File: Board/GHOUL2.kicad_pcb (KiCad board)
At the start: 2 copper layers, 105.4 x 88.9 mm, 37 parts

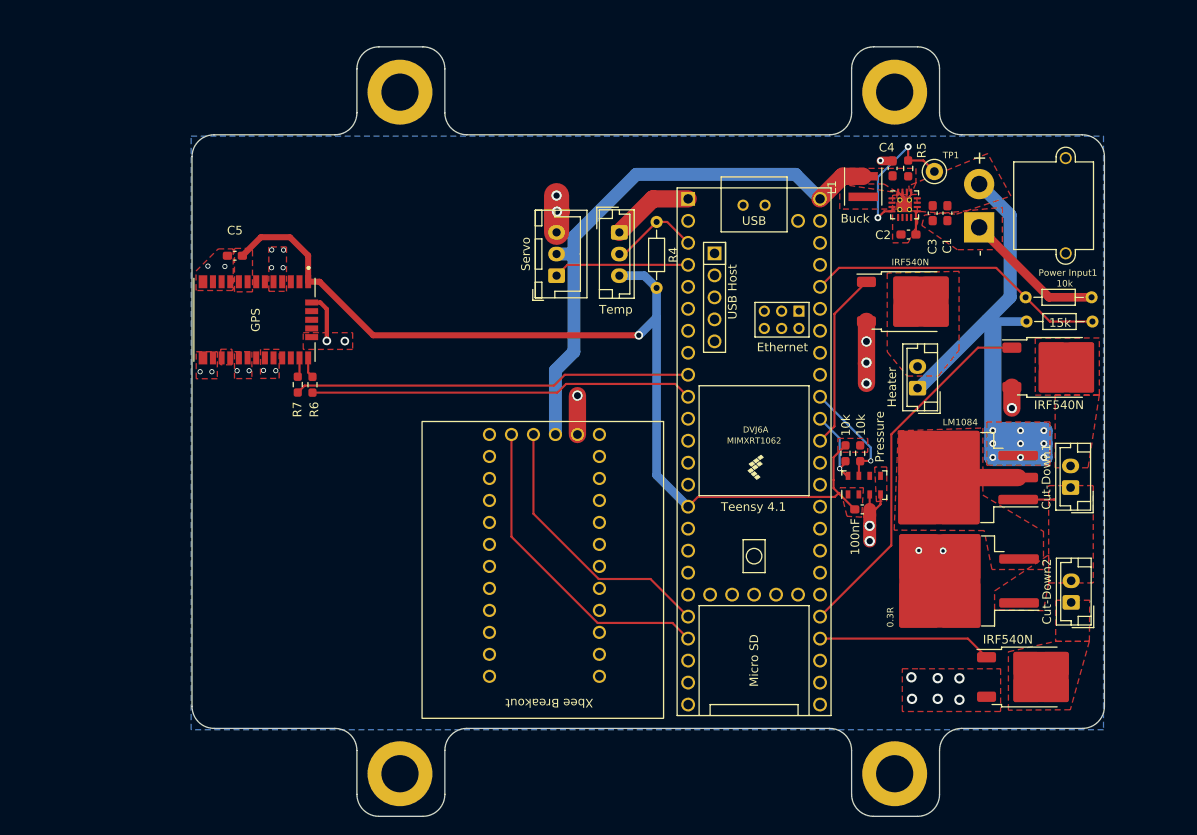
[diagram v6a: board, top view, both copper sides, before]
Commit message: added SAM and changed PCB
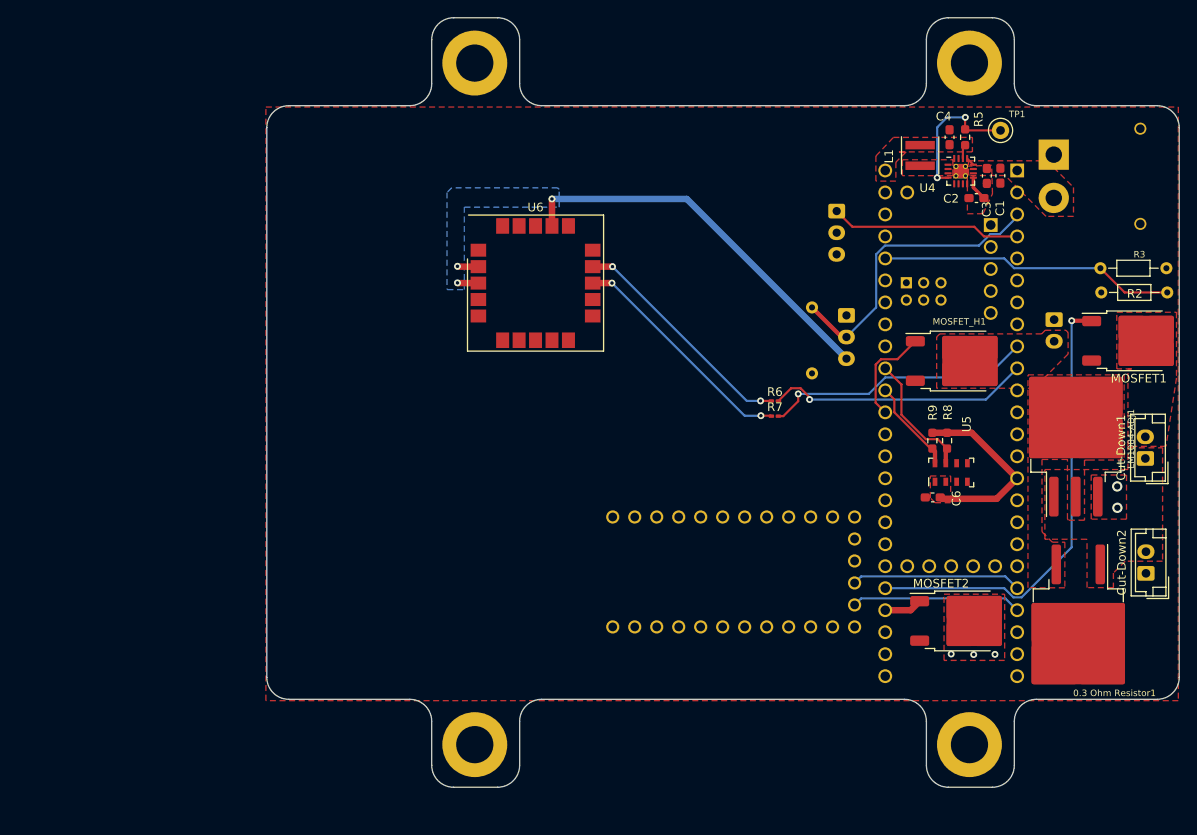
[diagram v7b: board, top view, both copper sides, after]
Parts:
- removed C5: 4.7uF, Capacitor_SMD:C_0603_1608Metric_Pad1.08x0.95mm_HandSolder
- removed GPS: CAM-M8Q-0, CAM-M8Q-0:LCC100P960X1400X210-31N
- added U6: SAM-M8Q, RF_GPS:ublox_SAM-M8Q, F.Cu at (133.8, 85.6)
- 0.3 Ohm Resistor1: renamed from 0.3R
- M1: renamed from Servo; moved to B.Cu
- Power Input1: moved to B.Cu
- R1: renamed from Heater; moved to B.Cu
- R2: renamed from 15k; value 15K -> 15k
- R4: moved to B.Cu
- R6, R7: value 220 -> R220; footprint Resistor_SMD:R_0603_1608Metric_Pad0.98x0.95mm_HandSolder -> Resistor_SMD:R_0201_0603Metric_Pad0.64x0.40mm_HandSolder
- U1: renamed from Teensy 4.1; moved to B.Cu
- U2: renamed from Temp; moved to B.Cu
- Xbee Breakout1: renamed from Xbee Breakout; moved to B.Cu
- moved R7 55.2 mm to (161.4, 100.9), turned to 0 degrees
- moved R6 53.5 mm to (161.4, 99.2), turned to 0 degrees
- moved M1 33.2 mm to (168.6, 77.2), turned to -90 degrees
- moved U2 27.9 mm to (169.7, 89.3)
- moved Xbee Breakout1 23.8 mm to (172.1, 105.2), turned to -90 degrees
- moved U1 23.0 mm to (181.8, 101.8)
- moved R4 20.5 mm to (165.7, 88.4)
- moved G*** 18.0 mm to (142.1, 91.8), turned to 0 degrees
- moved R1 17.7 mm to (193.7, 89.8), turned to -90 degrees
- moved 0.3 Ohm Resistor1 15.6 mm to (196.5, 125.7), turned to -90 degrees
- moved LM1084-ADJ1 15.3 mm to (196.2, 102.6), turned to 90 degrees
- moved Power Input1 12.0 mm to (193.6, 70.7), turned to 90 degrees
- moved R9 10.1 mm to (179.6, 103.8)
- moved R8 10.1 mm to (181.3, 103.8)
- moved U5 10.1 mm to (181.8, 107.4)
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- renumbered 100nF to C6, LM1084 to LM1084-ADJ1, IRF540N to MOSFET1, IRF540N to MOSFET2, IRF540N to MOSFET_H1, 10k to R3, 10k to R8, 10k to R9, Buck to U4, Pressure to U5
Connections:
- R6 pad 1: GPSRx -> Net-(U6-RXD)
- R6 pad 2: Net-(U3-RXD/SPI_MOSI) -> GPSRx
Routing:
- net +BATT: track 71.4 -> 1.01 mm, vias 9 -> 2
- net +5V: track 64.4 -> 1.65 mm
- net GND: track 63.1 -> 0.40 mm, vias 32 -> 0
- net +3.3V: track 114.7 -> 71.6 mm, vias 1 -> 3
- net Net-(U6-RXD): track 0.00 -> 27.1 mm, vias 0 -> 2
- net Net-(U6-TXD): track 2.26 -> 27.0 mm, vias 0 -> 2
- net Temp_Data: track 10.5 -> 34.7 mm
- net Xbee DIn: track 37.1 -> 19.7 mm
- net Nic2: track 20.1 -> 4.41 mm
- net GPSTx: track 45.9 -> 31.4 mm, vias 0 -> 1
- net GPSRx: track 44.4 -> 30.4 mm, vias 0 -> 1
- net Xbee DOut: track 31.9 -> 19.7 mm
- net Nic1: track 42.5 -> 52.9 mm, vias 0 -> 1
- net Net-(MOSFET_H1-G): track 20.6 -> 11.7 mm
- net Net-(LM1084-ADJ1-VO): track 9.15 -> 0.78 mm
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- added copper zone on B.Cu, net +3.3V
- added copper zone on In2.Cu, net +3.3V
- added copper zone on In2.Cu, net +5V
- added copper zone on In2.Cu, net +BATT
- added copper zone on In1.Cu, net GND
- added copper zone on In2.Cu, net Net-(Cut-Down2-In)
- removed copper zone on B.Cu, net GND
- removed copper zone on F.Cu, net Net-(U3-RF_IN)
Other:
- copper layers 2 -> 4

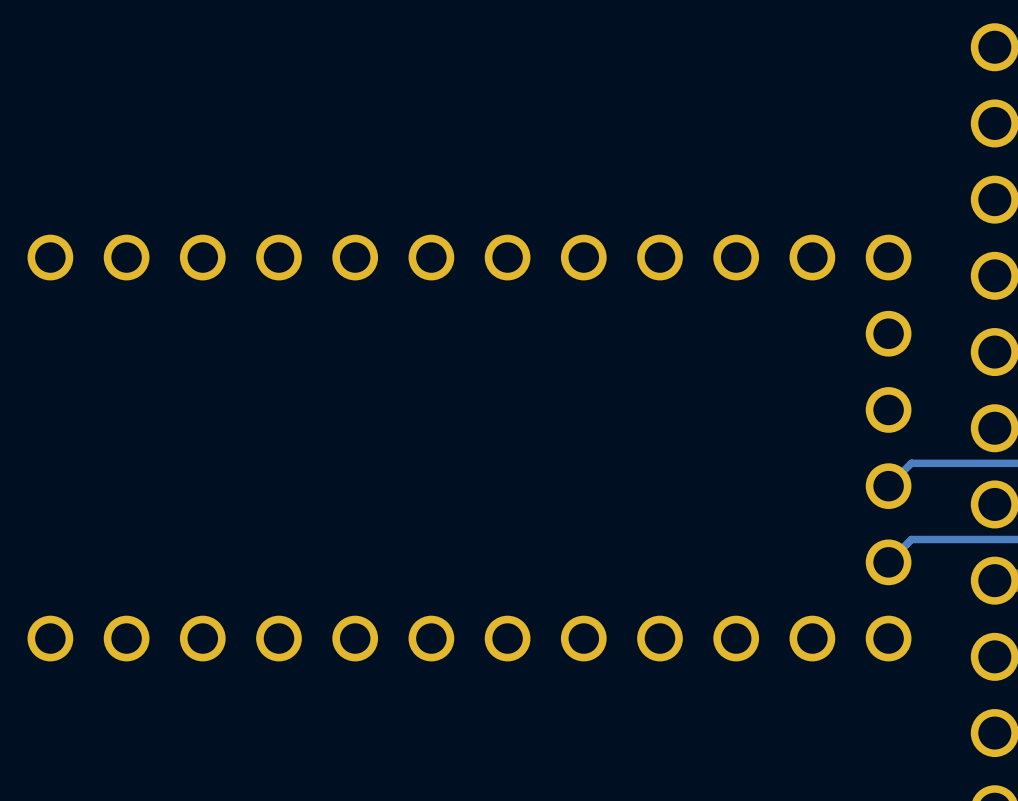
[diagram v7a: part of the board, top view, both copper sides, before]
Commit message: added teensy rtc
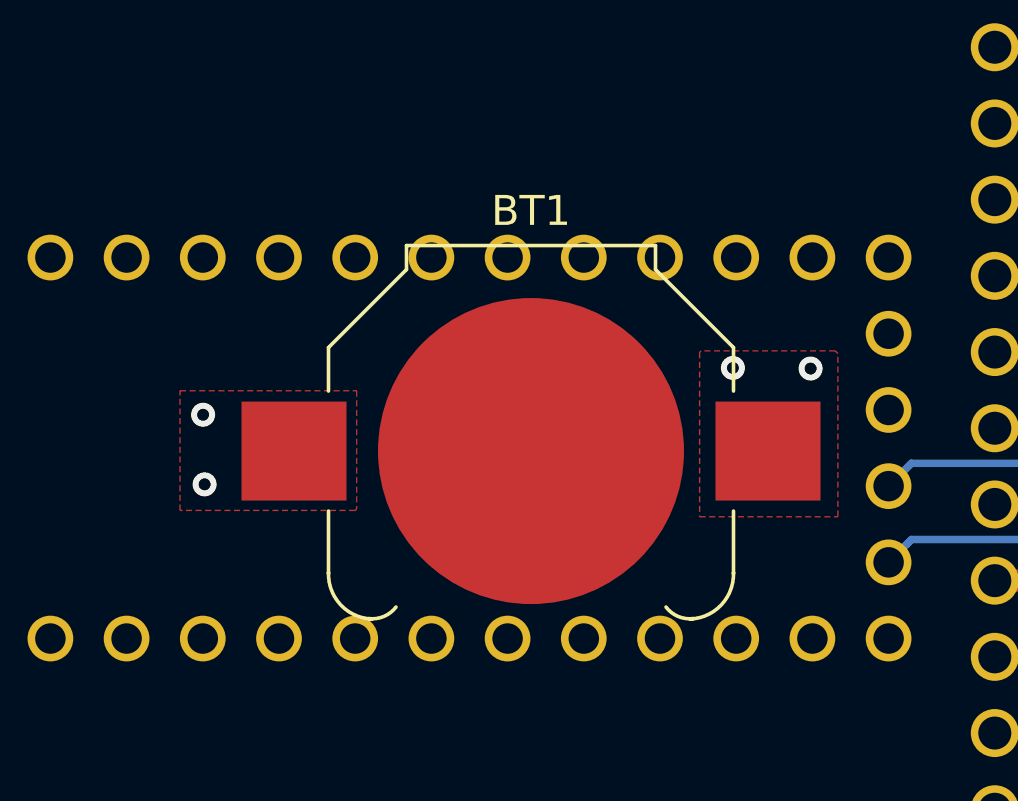
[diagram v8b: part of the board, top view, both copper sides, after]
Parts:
- added BT1: Battery_Cell, Battery:BatteryHolder_Keystone_3000_1x12mm, F.Cu at (158.7, 119.0)
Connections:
- U1 pad 50: unconnected-(U1-VBAT-Pad50) -> RTC_BATT
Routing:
- net RTC_BATT: track 0.00 -> 0.64 mm, vias 0 -> 4
- added copper zone on F.Cu, net RTC_BATT
- added copper zone on In2.Cu, net RTC_BATT
